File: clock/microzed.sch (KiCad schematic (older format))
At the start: 13 parts, among them U401 74LVC541

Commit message: Checkpoint... Pin swaps on microzed connector.
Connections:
- net labels added: PX1_LVDS_10_P, PX1_LVDS_2_N, PX1_LVDS_2_P, PX1_LVDS_4_N, PX1_LVDS_8_N
- net labels removed: PX1_LVDS_1_N, PX1_LVDS_1_P, PX1_LVDS_3_N, PX1_LVDS_3_P, PX1_LVDS_7_N
- wire segments 240 -> 232
- no-connect marks 113 -> 106
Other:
- moved on the sheet: R402, R403, R404, R405, R406

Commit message: Place the reference designators.
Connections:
- no-connect marks 106 -> 105
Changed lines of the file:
@@
 Text Label 4650 1450 0    40   ~ 0
 ~CARRIER_SRST~
-NoConn ~ 4550 1450
 Wire Wire Line
 	5300 1650 4550 1650
@@
 PX1_LVDS_10_P
 NoConn ~ 6650 3250
+Text HLabel 4550 1450 0    60   Input ~ 0
+~CARRIER_SRST~
 $EndSCHEMATC

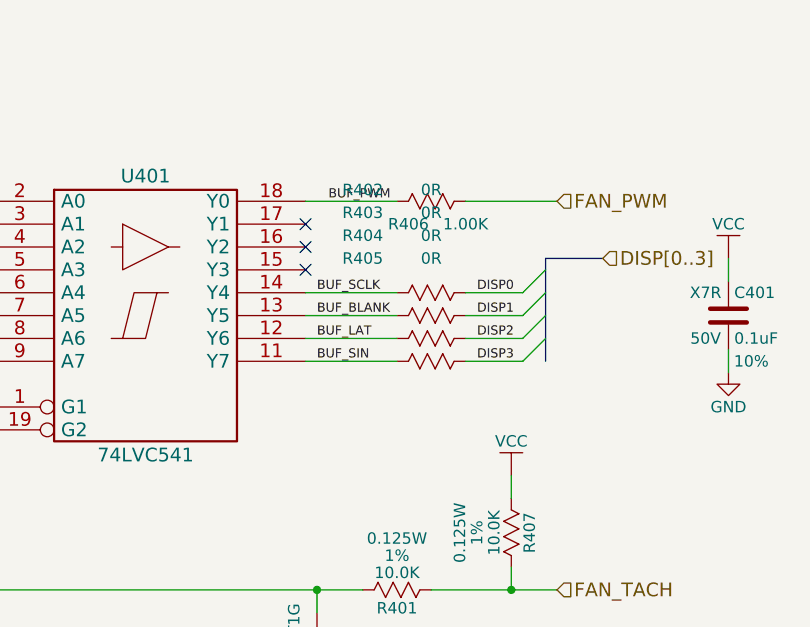
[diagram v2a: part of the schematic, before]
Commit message: Lock all the stitching vias. Remove FVXO alternate to OCXO.
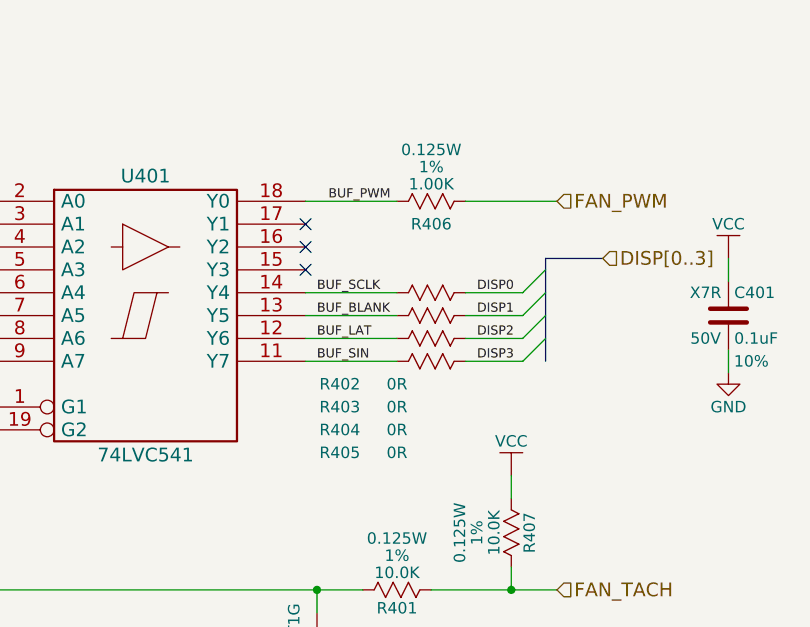
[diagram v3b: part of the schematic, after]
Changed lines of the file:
@@
 $EndDescr
 $Comp
-L GND #PWR050
+L GND #PWR046
 U 1 1 5623DA38
 P 3000 6250
-F 0 "#PWR050" H 3000 6000 50  0001 C CNN
+F 0 "#PWR046" H 3000 6000 50  0001 C CNN
 F 1 "GND" H 3000 6100 50  0000 C CNN
 F 2 "" H 3000 6250 60  0000 C CNN
@@
 $EndComp
 $Comp
-L GND #PWR051
+L GND #PWR047
 U 1 1 5623DA70
 P 2200 6250
-F 0 "#PWR051" H 2200 6000 50  0001 C CNN
+F 0 "#PWR047" H 2200 6000 50  0001 C CNN
 F 1 "GND" H 2200 6100 50  0000 C CNN
 F 2 "" H 2200 6250 60  0000 C CNN
@@
 $EndComp
 $Comp
-L GND #PWR052
+L GND #PWR048
 U 1 1 5623DAE1
 P 6000 6250
-F 0 "#PWR052" H 6000 6000 50  0001 C CNN
+F 0 "#PWR048" H 6000 6000 50  0001 C CNN
 F 1 "GND" H 6000 6100 50  0000 C CNN
 F 2 "" H 6000 6250 60  0000 C CNN
@@
 $EndComp
 $Comp
-L GND #PWR053
+L GND #PWR049
 U 1 1 5623DB66
 P 5200 6250
-F 0 "#PWR053" H 5200 6000 50  0001 C CNN
+F 0 "#PWR049" H 5200 6000 50  0001 C CNN
 F 1 "GND" H 5200 6100 50  0000 C CNN
 F 2 "" H 5200 6250 60  0000 C CNN
@@
 	2300 1750 2000 1750
 $Comp
-L VIN #PWR054
+L VIN #PWR050
 U 1 1 5623ED14
 P 2000 1750
-F 0 "#PWR054" H 2000 1600 50  0001 C CNN
+F 0 "#PWR050" H 2000 1600 50  0001 C CNN
 F 1 "VIN" V 2000 1925 50  0000 C CNN
 F 2 "" H 2000 1750 60  0000 C CNN
@@
 $EndComp
 $Comp
-L VIN #PWR055
+L VIN #PWR051
 U 1 1 5623ED8A
 P 2000 4050
-F 0 "#PWR055" H 2000 3900 50  0001 C CNN
+F 0 "#PWR051" H 2000 3900 50  0001 C CNN
 F 1 "VIN" V 2000 4225 50  0000 C CNN
 F 2 "" H 2000 4050 60  0000 C CNN
@@
 $EndComp
 $Comp
-L VIN #PWR056
+L VIN #PWR052
 U 1 1 5623EE30
 P 3200 4050
-F 0 "#PWR056" H 3200 3900 50  0001 C CNN
+F 0 "#PWR052" H 3200 3900 50  0001 C CNN
 F 1 "VIN" V 3200 4225 50  0000 C CNN
 F 2 "" H 3200 4050 60  0000 C CNN
@@
 $EndComp
 $Comp
-L VIN #PWR057
+L VIN #PWR053
 U 1 1 5623EEAF
 P 5000 4050
-F 0 "#PWR057" H 5000 3900 50  0001 C CNN
+F 0 "#PWR053" H 5000 3900 50  0001 C CNN
 F 1 "VIN" V 5000 4225 50  0000 C CNN
 F 2 "" H 5000 4050 60  0000 C CNN
@@
 $EndComp
 $Comp
-L VIN #PWR058
+L VIN #PWR054
 U 1 1 5623EF12
 P 6200 4050
-F 0 "#PWR058" H 6200 3900 50  0001 C CNN
+F 0 "#PWR054" H 6200 3900 50  0001 C CNN
 F 1 "VIN" V 6200 4225 50  0000 C CNN
 F 2 "" H 6200 4050 60  0000 C CNN
@@
 Connection ~ 5100 5050
 $Comp
-L VCCO #PWR059
+L VCCO #PWR055
 U 1 1 5623F518
 P 6200 5150
-F 0 "#PWR059" H 6200 5000 50  0001 C CNN
+F 0 "#PWR055" H 6200 5000 50  0001 C CNN
 F 1 "VCCO" V 6200 5350 50  0000 C CNN
 F 2 "" H 6200 5150 60  0000 C CNN
@@
 Connection ~ 2100 5050
 $Comp
-L VCCO #PWR060
+L VCCO #PWR056
 U 1 1 5623F63E
 P 2000 5050
-F 0 "#PWR060" H 2000 4900 50  0001 C CNN
+F 0 "#PWR056" H 2000 4900 50  0001 C CNN
 F 1 "VCCO" V 2000 5250 50  0000 C CNN
 F 2 "" H 2000 5050 60  0000 C CNN
@@
 	2900 5150 3200 5150
 $Comp
-L VCCO #PWR061
+L VCCO #PWR057
 U 1 1 5623F67B
 P 3200 5150
-F 0 "#PWR061" H 3200 5000 50  0001 C CNN
+F 0 "#PWR057" H 3200 5000 50  0001 C CNN
 F 1 "VCCO" V 3200 5350 50  0000 C CNN
 F 2 "" H 3200 5150 60  0000 C CNN
@@
 	2300 6050 2000 6050
 $Comp
-L VCCO #PWR062
+L VCCO #PWR058
 U 1 1 5623F755
 P 2000 6050
-F 0 "#PWR062" H 2000 5900 50  0001 C CNN
+F 0 "#PWR058" H 2000 5900 50  0001 C CNN
 F 1 "VCCO" V 2000 6250 50  0000 C CNN
 F 2 "" H 2000 6050 60  0000 C CNN
@@
 3DFIX
 $Comp
-L VIN #PWR063
+L VIN #PWR059
 U 1 1 562597FE
 P 1100 750
-F 0 "#PWR063" H 1100 600 50  0001 C CNN
+F 0 "#PWR059" H 1100 600 50  0001 C CNN
 F 1 "VIN" H 1100 900 50  0000 C CNN
 F 2 "" H 1100 750 60  0000 C CNN
@@
 	1100 850  1100 750
 $Comp
-L VCCO #PWR064
+L VCCO #PWR060
 U 1 1 562598AE
 P 1900 750
-F 0 "#PWR064" H 1900 600 50  0001 C CNN
+F 0 "#PWR060" H 1900 600 50  0001 C CNN
 F 1 "VCCO" H 1900 900 50  0000 C CNN
 F 2 "" H 1900 750 60  0000 C CNN
@@
 	1900 850  1900 750
 $Comp
-L GND #PWR065
+L GND #PWR061
 U 1 1 56259970
 P 2950 750
-F 0 "#PWR065" H 2950 500 50  0001 C CNN
+F 0 "#PWR061" H 2950 500 50  0001 C CNN
 F 1 "GND" H 2950 600 50  0000 C CNN
 F 2 "" H 2950 750 60  0000 C CNN
@@
 DISP3
 $Comp
-L VCC #PWR066
+L VCC #PWR062
 U 1 1 56368B50
 P 2150 750
-F 0 "#PWR066" H 2150 600 50  0001 C CNN
+F 0 "#PWR062" H 2150 600 50  0001 C CNN
 F 1 "VCC" H 2150 900 50  0000 C CNN
 F 2 "" H 2150 750 60  0000 C CNN
@@
 U 1 1 563694E5
 P 9650 1750
-F 0 "R402" V 9200 1450 50  0000 C CNN
-F 1 "0R" V 9200 1750 50  0000 C CNN
+F 0 "R402" V 10050 1350 50  0000 C CNN
+F 1 "0R" V 10050 1600 50  0000 C CNN
 F 2 "Resistors_SMD:R_0805_HandSoldering" V 9580 1750 30  0001 C CNN
 F 3 "" V 9730 1750 30  0000 C CNN
@@
 U 1 1 5636980F
 P 9650 1350
-F 0 "R406" V 9750 1250 50  0000 C CNN
-F 1 "1.00K" V 9750 1500 50  0000 C CNN
+F 0 "R406" V 9750 1350 50  0000 C CNN
+F 1 "1.00K" V 9575 1350 50  0000 C CNN
 F 2 "Resistors_SMD:R_0805_HandSoldering" V 9580 1350 30  0001 C CNN
 F 3 "" V 9730 1350 30  0000 C CNN
-F 4 "1%" V 9500 1350 50  0001 C CNN "Tolerance"
-F 5 "0.125W" V 9425 1350 50  0001 C CNN "Power"
+F 4 "1%" V 9500 1350 50  0000 C CNN "Tolerance"
+F 5 "0.125W" V 9425 1350 50  0000 C CNN "Power"
 F 6 "Vishay Dale" V 9650 1350 50  0001 C CNN "Manufacturer"
 F 7 "CRCW08051K00FKEA" V 9800 1350 50  0001 C CNN "PartNum"
@@
 Connection ~ 7500 2350
 $Comp
-L GND #PWR067
+L GND #PWR063
 U 1 1 56369E58
 P 7500 2450
-F 0 "#PWR067" H 7500 2200 50  0001 C CNN
+F 0 "#PWR063" H 7500 2200 50  0001 C CNN
 F 1 "GND" H 7500 2300 50  0000 C CNN
 F 2 "" H 7500 2450 60  0000 C CNN
@@
 	9150 3050 9150 3150
 $Comp
-L VCC #PWR068
+L VCC #PWR064
 U 1 1 563911B0
 P 10000 2550
-F 0 "#PWR068" H 10000 2400 50  0001 C CNN
+F 0 "#PWR064" H 10000 2400 50  0001 C CNN
 F 1 "VCC" H 10000 2700 50  0000 C CNN
 F 2 "" H 10000 2550 60  0000 C CNN
@@
 $EndComp
 $Comp
-L GND #PWR069
+L GND #PWR065
 U 1 1 563911DC
 P 9150 3650
-F 0 "#PWR069" H 9150 3400 50  0001 C CNN
+F 0 "#PWR065" H 9150 3400 50  0001 C CNN
 F 1 "GND" H 9150 3500 50  0000 C CNN
 F 2 "" H 9150 3650 60  0000 C CNN
@@
 U 1 1 563F4285
 P 9650 1850
-F 0 "R403" V 9200 1550 50  0000 C CNN
-F 1 "0R" V 9200 1850 50  0000 C CNN
+F 0 "R403" V 10050 1450 50  0000 C CNN
+F 1 "0R" V 10050 1700 50  0000 C CNN
 F 2 "Resistors_SMD:R_0805_HandSoldering" V 9580 1850 30  0001 C CNN
 F 3 "" V 9730 1850 30  0000 C CNN
@@
 U 1 1 563F42BB
 P 9650 1950
-F 0 "R404" V 9200 1650 50  0000 C CNN
-F 1 "0R" V 9200 1950 50  0000 C CNN
+F 0 "R404" V 10050 1550 50  0000 C CNN
+F 1 "0R" V 10050 1800 50  0000 C CNN
 F 2 "Resistors_SMD:R_0805_HandSoldering" V 9580 1950 30  0001 C CNN
 F 3 "" V 9730 1950 30  0000 C CNN
@@
 U 1 1 563F42F4
 P 9650 2050
-F 0 "R405" V 9200 1750 50  0000 C CNN
-F 1 "0R" V 9200 2050 50  0000 C CNN
+F 0 "R405" V 10050 1650 50  0000 C CNN
+F 1 "0R" V 10050 1900 50  0000 C CNN
 F 2 "Resistors_SMD:R_0805_HandSoldering" V 9580 2050 30  0001 C CNN
 F 3 "" V 9730 2050 30  0000 C CNN
@@
 NoConn ~ 9100 1650
 $Comp
-L VCCO #PWR070
+L VCCO #PWR066
 U 1 1 563E2413
 P 5000 5050
-F 0 "#PWR070" H 5000 4900 50  0001 C CNN
+F 0 "#PWR066" H 5000 4900 50  0001 C CNN
 F 1 "VCCO" V 5000 5250 50  0000 C CNN
 F 2 "" H 5000 5050 60  0000 C CNN
@@
 TACH
 $Comp
-L GND #PWR071
+L GND #PWR067
 U 1 1 56403C33
 P 10950 2100
-F 0 "#PWR071" H 10950 1850 50  0001 C CNN
+F 0 "#PWR067" H 10950 1850 50  0001 C CNN
 F 1 "GND" H 10950 1950 50  0000 C CNN
 F 2 "" H 10950 2100 60  0000 C CNN
@@
 $EndComp
 $Comp
-L VCC #PWR072
+L VCC #PWR068
 U 1 1 56403C47
 P 10950 1600
-F 0 "#PWR072" H 10950 1450 50  0001 C CNN
+F 0 "#PWR068" H 10950 1450 50  0001 C CNN
 F 1 "VCC" H 10950 1750 50  0000 C CNN
 F 2 "" H 10950 1600 60  0000 C CNN

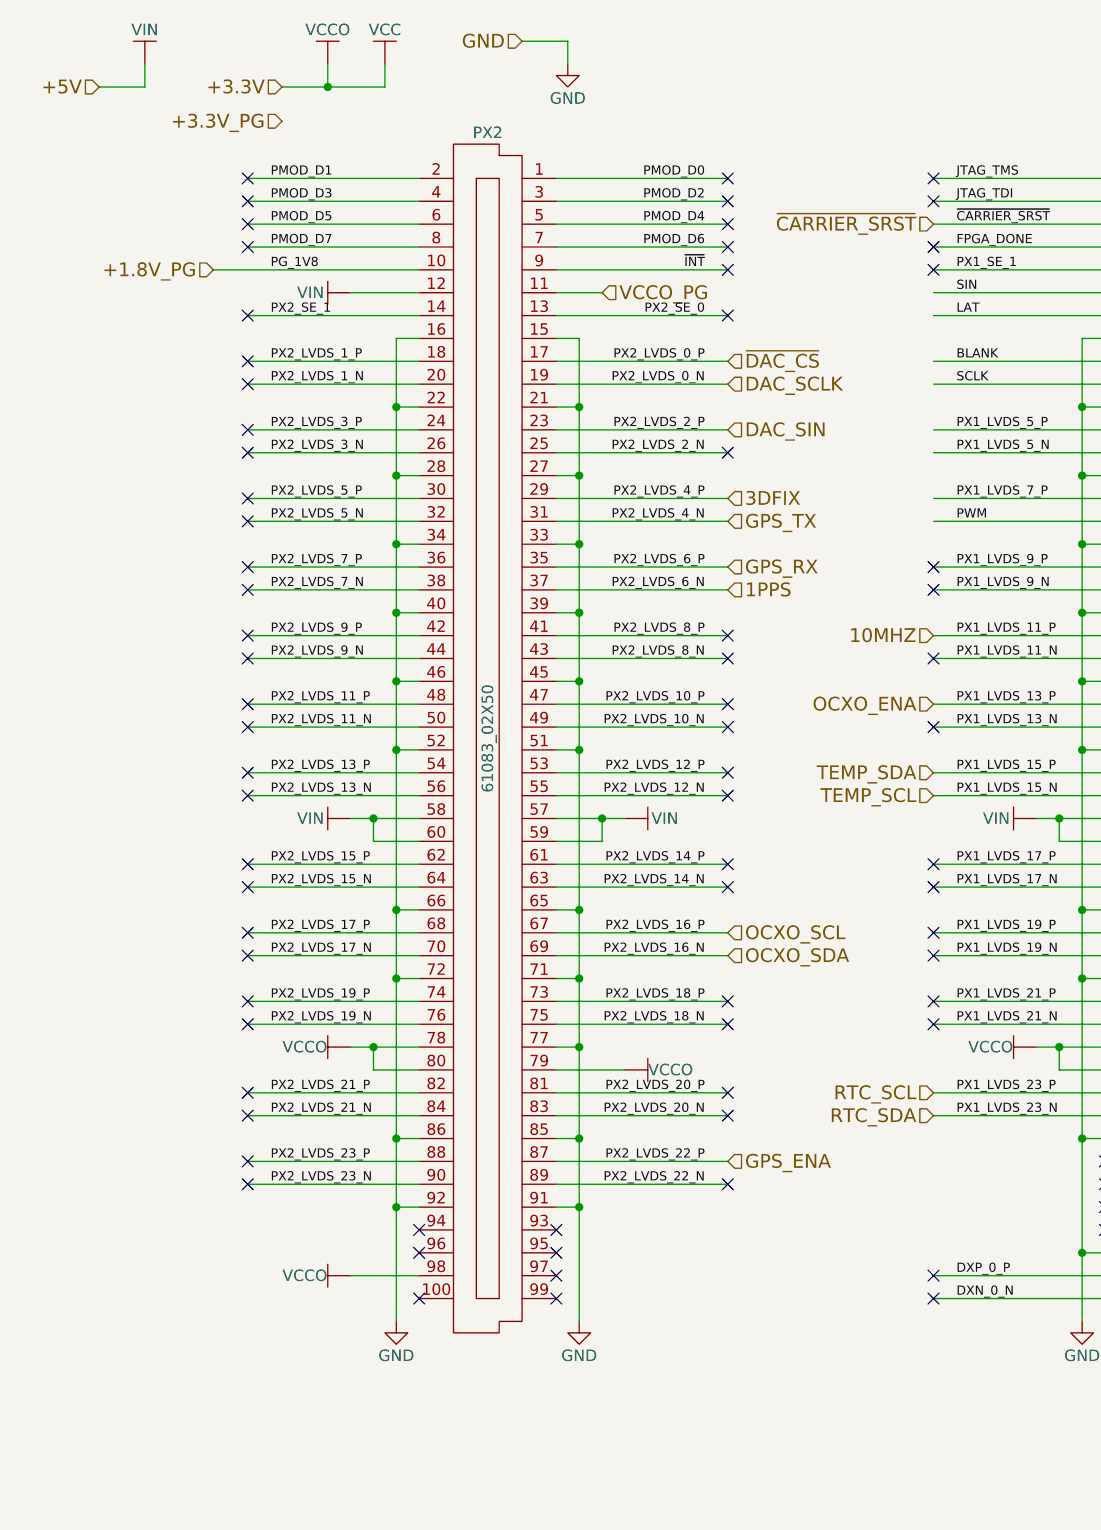
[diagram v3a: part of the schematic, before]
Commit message: Checkpoint pin swaps and addition of 3D models.
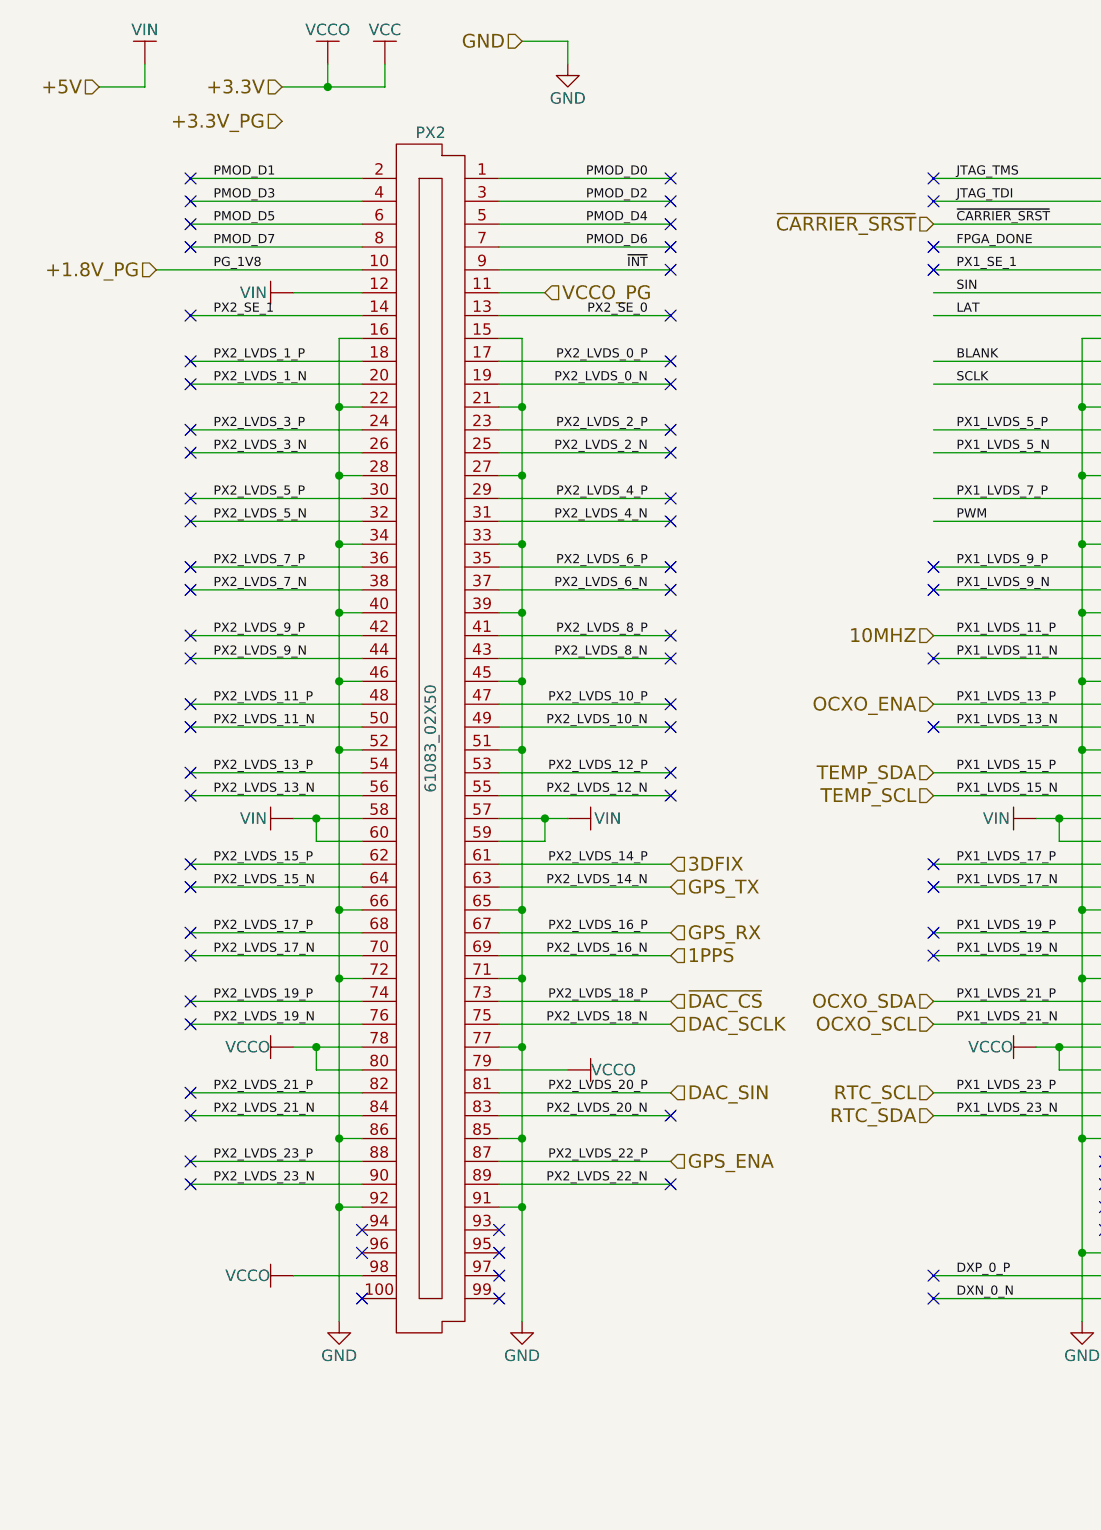
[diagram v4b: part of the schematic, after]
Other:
- moved on the sheet: PX2
